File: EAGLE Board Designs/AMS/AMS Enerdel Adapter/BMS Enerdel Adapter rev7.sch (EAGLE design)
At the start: 30 parts, among them J1 CONNECTOR-1_5222_, J10 CONNECTOR-1_5222_, J11 CONNECTOR-1_5222_, J12 CONNECTOR-1_5222_, J13 CONNECTOR-1_5222_, J14 CONNECTOR-1_5222_, J15 CONNECTOR-1_5222_, J16 CONNECTOR-1_5222_, J17 CONNECTOR-1_5222_, J18 CONNECTOR-1_5222_, J19 CONNECTOR-1_5222_, J2 CONNECTOR-1_5222_, J20 CONNECTOR-1_5222_, J21 CONNECTOR-1_5222_, J22 CONNECTOR-1_5222_, J3 CONNECTOR-1_5222_, J4 CONNECTOR-1_5222_, J5 CONNECTOR-1_5222_, J6 CONNECTOR-1_5222_, J7 CONNECTOR-1_5222_, J8 CONNECTOR-1_5222_, J9 CONNECTOR-1_5222_

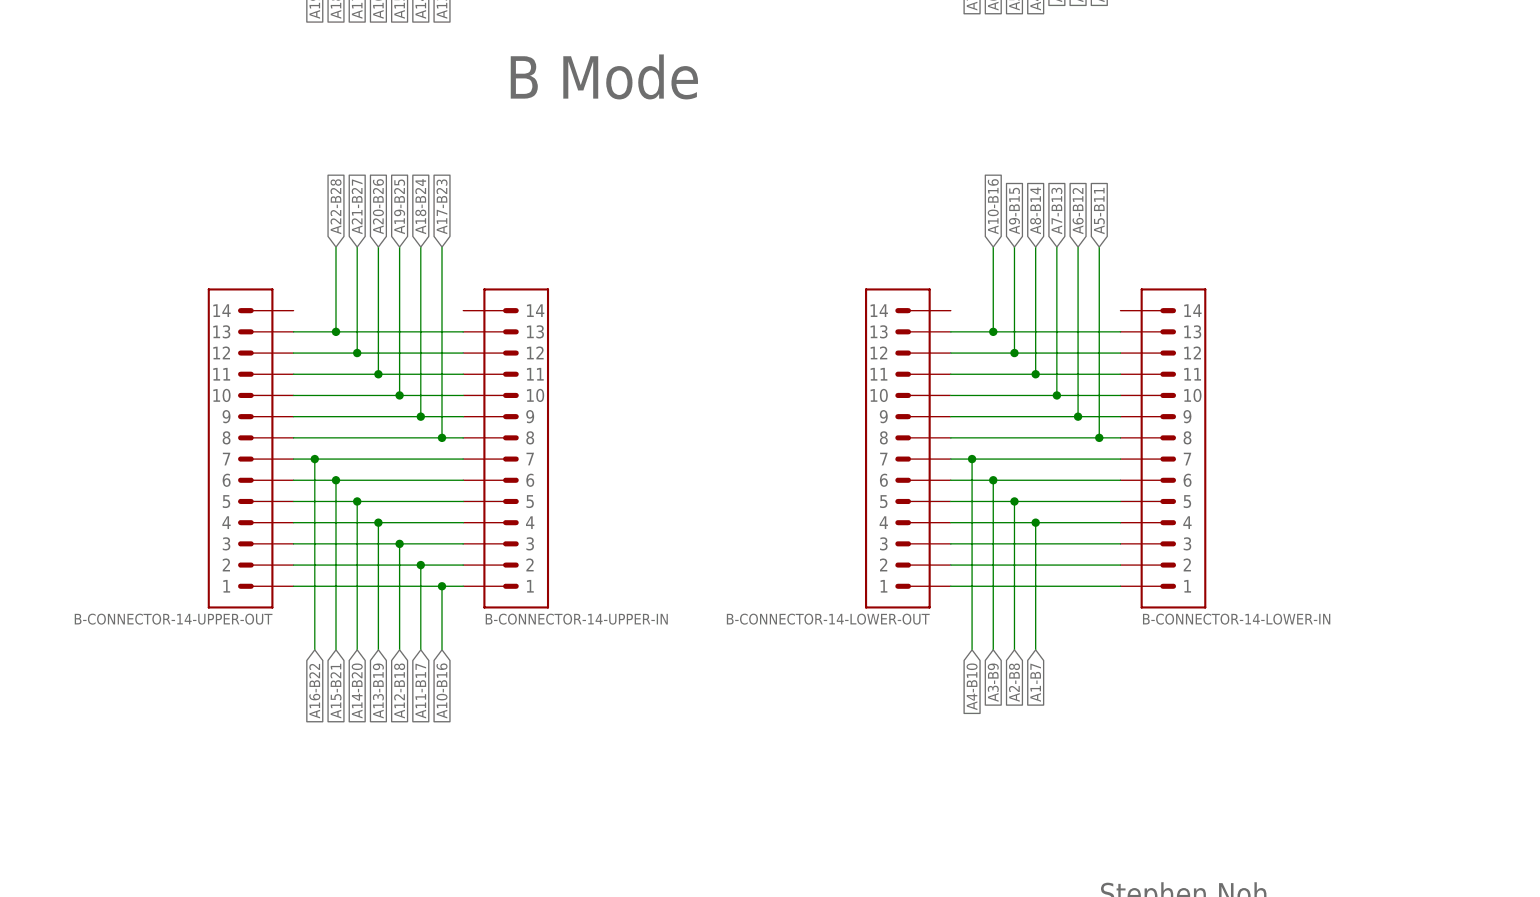
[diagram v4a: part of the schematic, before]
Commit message: Removed mode b, changed silkscreen
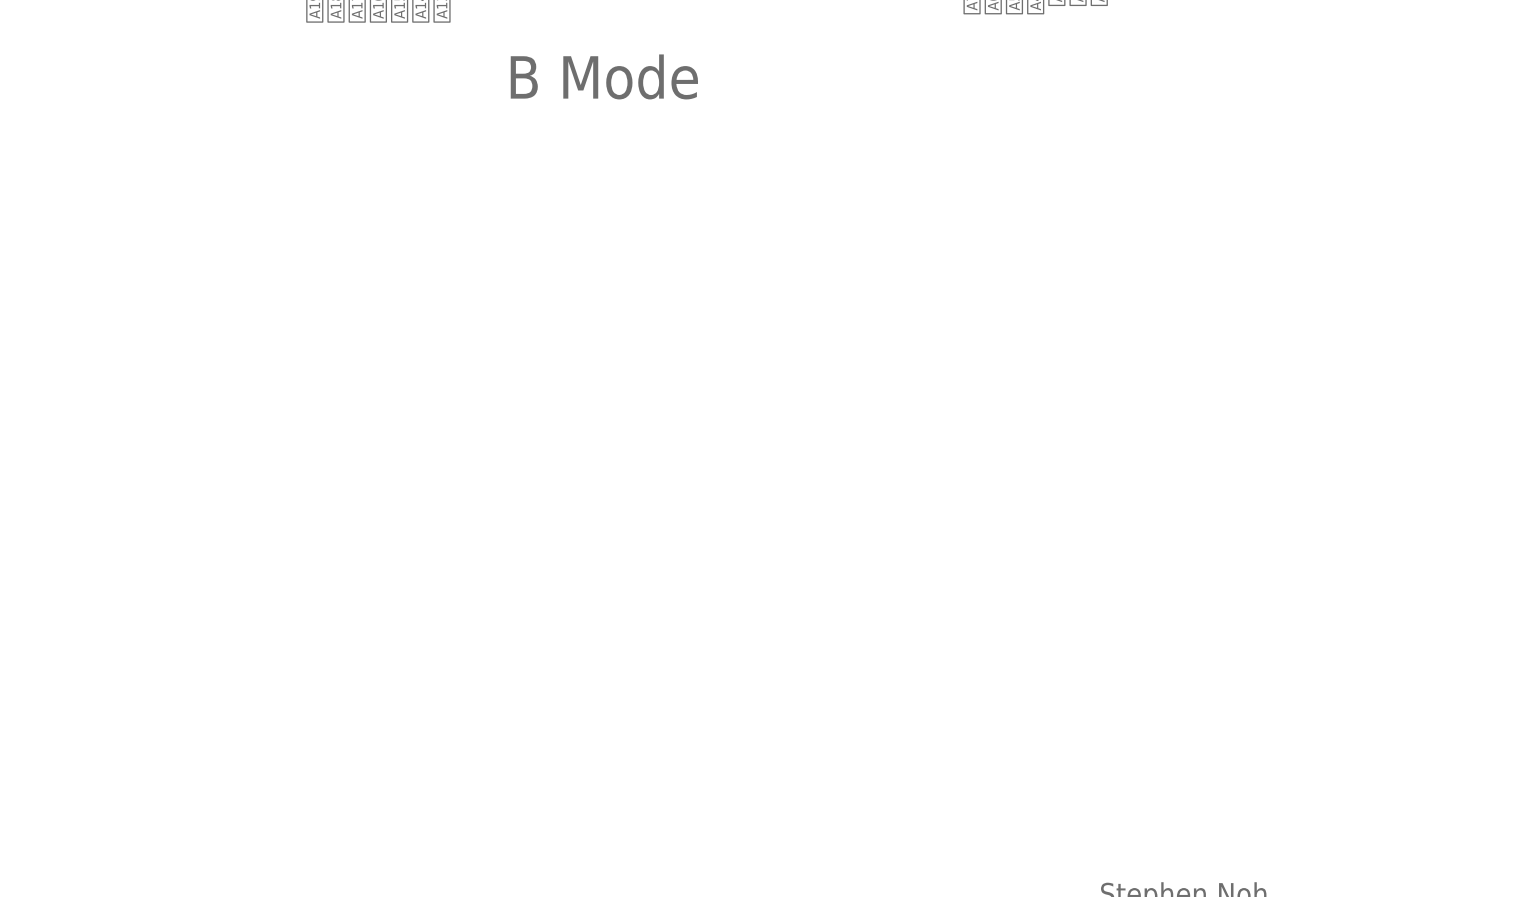
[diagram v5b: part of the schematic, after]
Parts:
- removed B-CONNECTOR-14-LOWER-IN, B-CONNECTOR-14-LOWER-OUT: CONNECTOR-14_MINIFIT_, HyTechDevices:CONNECTOR-14_MINIFIT_
- removed B-CONNECTOR-14-UPPER-IN, B-CONNECTOR-14-UPPER-OUT: CONNECTOR-14_NANOFIT_, HyTechDevices:CONNECTOR-14_NANOFIT_
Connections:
- removed net B-PASS1: B-CONNECTOR-14-LOWER-IN.3, B-CONNECTOR-14-LOWER-OUT.3
- removed net B-PASS2: B-CONNECTOR-14-LOWER-IN.2, B-CONNECTOR-14-LOWER-OUT.2
- removed net B-PASS3: B-CONNECTOR-14-LOWER-IN.1, B-CONNECTOR-14-LOWER-OUT.1
- net A1-B7: no longer B-CONNECTOR-14-LOWER-IN.4, B-CONNECTOR-14-LOWER-OUT.4
- net A10-B16: no longer B-CONNECTOR-14-LOWER-IN.13, B-CONNECTOR-14-LOWER-OUT.13, B-CONNECTOR-14-UPPER-IN.1, B-CONNECTOR-14-UPPER-OUT.1
- net A11-B17: no longer B-CONNECTOR-14-UPPER-IN.2, B-CONNECTOR-14-UPPER-OUT.2
- net A12-B18: no longer B-CONNECTOR-14-UPPER-IN.3, B-CONNECTOR-14-UPPER-OUT.3
- net A13-B19: no longer B-CONNECTOR-14-UPPER-IN.4, B-CONNECTOR-14-UPPER-OUT.4
- net A14-B20: no longer B-CONNECTOR-14-UPPER-IN.5, B-CONNECTOR-14-UPPER-OUT.5
- net A15-B21: no longer B-CONNECTOR-14-UPPER-IN.6, B-CONNECTOR-14-UPPER-OUT.6
- net A16-B22: no longer B-CONNECTOR-14-UPPER-IN.7, B-CONNECTOR-14-UPPER-OUT.7
- net A17-B23: no longer B-CONNECTOR-14-UPPER-IN.8, B-CONNECTOR-14-UPPER-OUT.8
- net A18-B24: no longer B-CONNECTOR-14-UPPER-IN.9, B-CONNECTOR-14-UPPER-OUT.9
- net A19-B25: no longer B-CONNECTOR-14-UPPER-IN.10, B-CONNECTOR-14-UPPER-OUT.10
- net A2-B8: no longer B-CONNECTOR-14-LOWER-IN.5, B-CONNECTOR-14-LOWER-OUT.5
- net A20-B26: no longer B-CONNECTOR-14-UPPER-IN.11, B-CONNECTOR-14-UPPER-OUT.11
- net A21-B27: no longer B-CONNECTOR-14-UPPER-IN.12, B-CONNECTOR-14-UPPER-OUT.12
- net A22-B28: no longer B-CONNECTOR-14-UPPER-IN.13, B-CONNECTOR-14-UPPER-OUT.13
- net A3-B9: no longer B-CONNECTOR-14-LOWER-IN.6, B-CONNECTOR-14-LOWER-OUT.6
- net A4-B10: no longer B-CONNECTOR-14-LOWER-IN.7, B-CONNECTOR-14-LOWER-OUT.7
- net A5-B11: no longer B-CONNECTOR-14-LOWER-IN.8, B-CONNECTOR-14-LOWER-OUT.8
- net A6-B12: no longer B-CONNECTOR-14-LOWER-IN.9, B-CONNECTOR-14-LOWER-OUT.9
- net A7-B13: no longer B-CONNECTOR-14-LOWER-IN.10, B-CONNECTOR-14-LOWER-OUT.10
- net A8-B14: no longer B-CONNECTOR-14-LOWER-IN.11, B-CONNECTOR-14-LOWER-OUT.11
- net A9-B15: no longer B-CONNECTOR-14-LOWER-IN.12, B-CONNECTOR-14-LOWER-OUT.12
